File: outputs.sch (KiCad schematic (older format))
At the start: 68 parts, among them J10 Conn_01x02_Male, J11 NO STUFF, J12 NO STUFF, J2 USB_B_Micro, J3 NO STUFF, J4 HDMI_A_1.4, J5 FH26W-45S-0.3SHW(60), J6 Conn_02x20_Odd_Even, J7 Conn_02x03_Odd_Even, J8 Conn_02x03_Odd_Even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

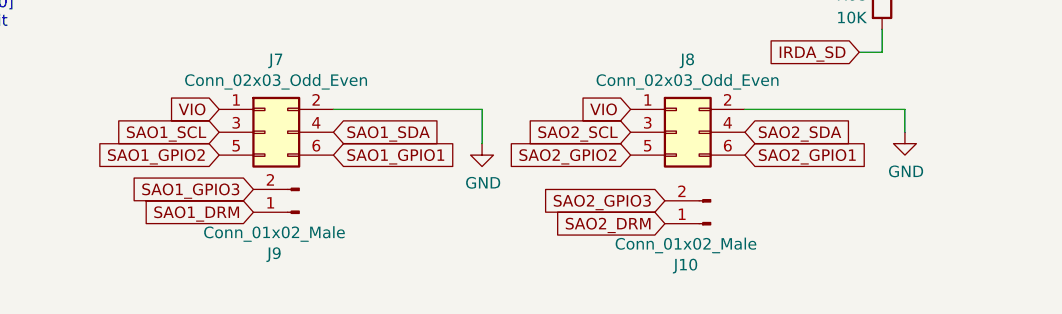
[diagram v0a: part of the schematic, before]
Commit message: Note oopsie in scl/sda
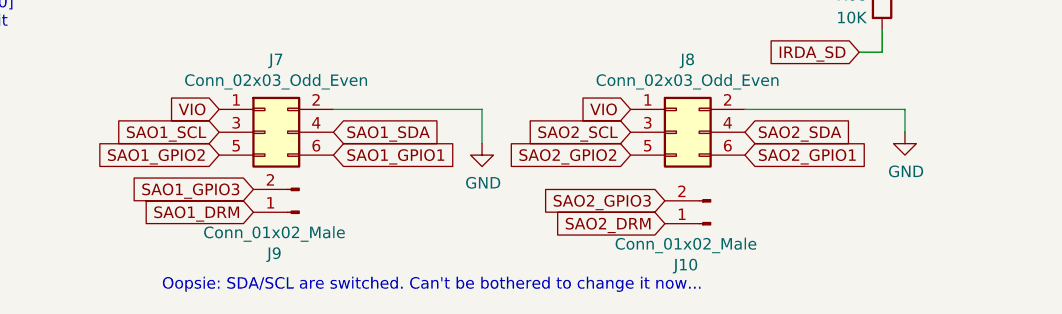
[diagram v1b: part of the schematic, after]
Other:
- note added: "Oopsie: SDA/SCL are switched. Can't be bothered to change it now..."
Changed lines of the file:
@@
 Text Notes 9000 4050 0    50   ~ 0
 Buttons are 6x6x4.3mm tactile things.
+Text Notes 3550 7400 0    50   ~ 0
+Oopsie: SDA/SCL are switched. Can't be bothered to change it now...
 $EndSCHEMATC
